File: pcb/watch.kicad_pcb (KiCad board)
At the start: 2 copper layers, 25.4 x 25.4 mm, 26 parts, among them SW1 EVP-AA202K, SW2 EVP-AA202K, U1 ATtiny402-SS

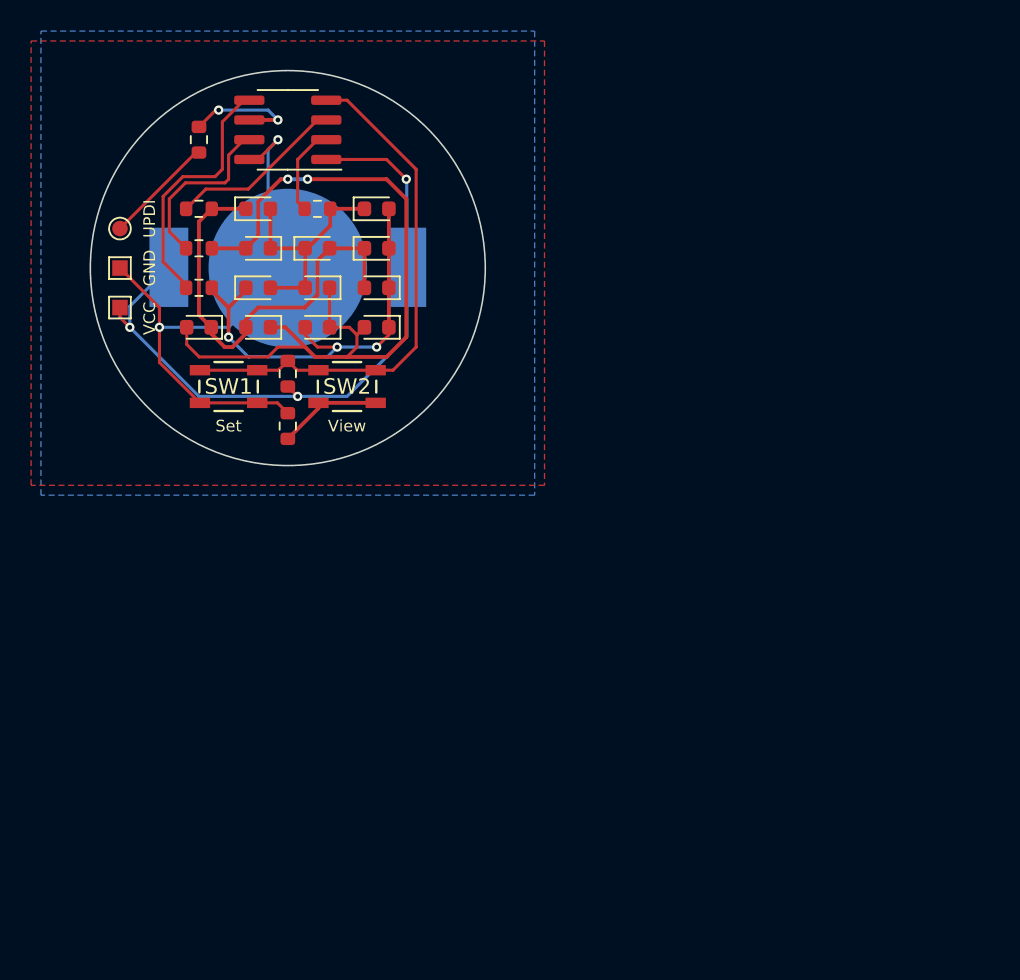
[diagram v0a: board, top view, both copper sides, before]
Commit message: Add alignment notch to PCB
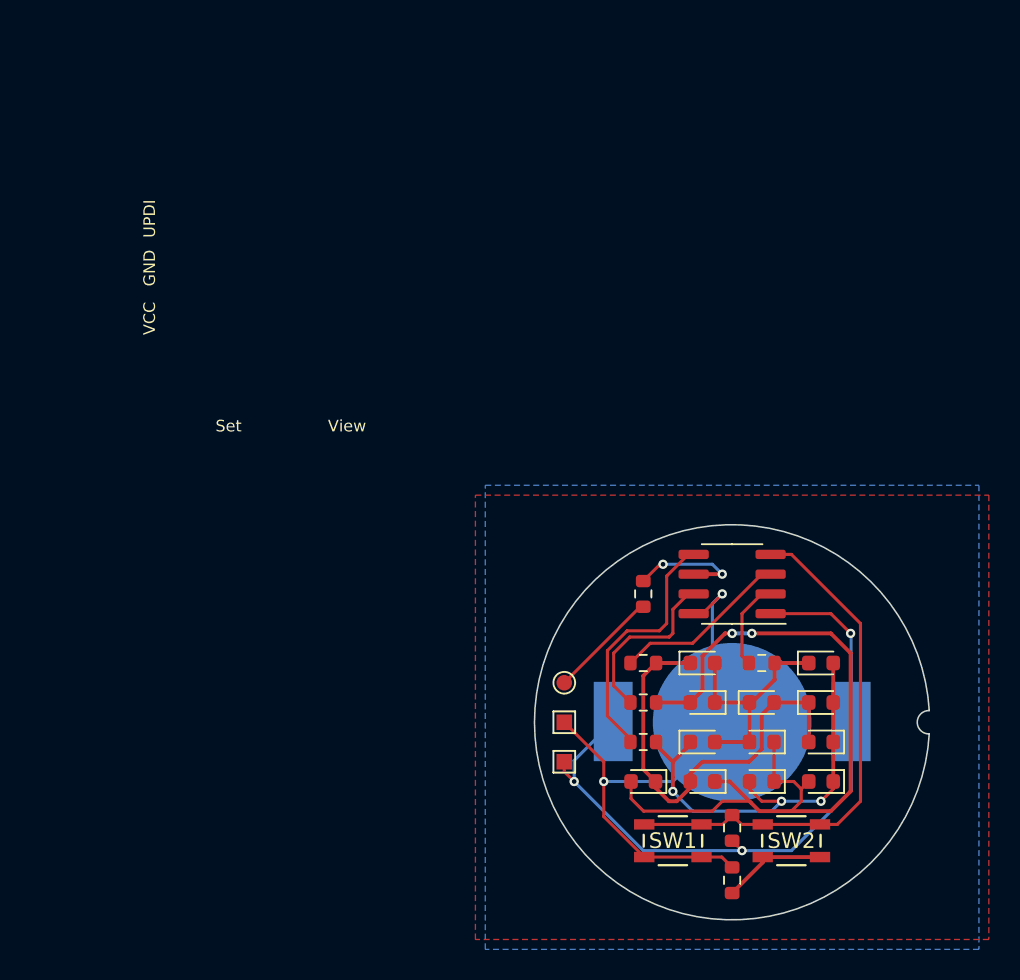
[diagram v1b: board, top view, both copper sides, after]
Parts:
- moved SW1 40.9 mm to (59.7, 71.1)
- moved SW2 40.9 mm to (67.3, 71.1)
- moved TP3 40.9 mm to (52.7, 66.0)
- moved BT1 40.9 mm to (63.5, 63.5)
- moved D1 40.9 mm to (65.4, 67.3)
- moved D10 40.9 mm to (61.6, 67.3)
- moved D2 40.9 mm to (69.2, 67.3)
- moved D7 40.9 mm to (69.2, 59.7)
- moved D9 40.9 mm to (57.8, 67.3)
- moved R3 40.9 mm to (65.4, 59.7)
- moved R5 40.9 mm to (63.5, 70.3)
- moved TP1 40.9 mm to (52.7, 61.0)
- moved TP2 40.9 mm to (52.7, 63.5)
- moved U1 40.9 mm to (63.5, 54.6)
- moved D11 40.9 mm to (69.2, 62.2)
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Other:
- outline, holes or cut-outs redrawn
